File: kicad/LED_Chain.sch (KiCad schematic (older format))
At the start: 14 parts

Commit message: Schematic and initial layout
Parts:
- removed D? (x2): LED, symbol Device:LED
- added J1: Conn_01x07_Male, Pin_Headers:Pin_Header_Angled_1x07_Pitch2.54mm, symbol Connector:Conn_01x07_Male
- added J2: L1, Connect:Banana_Jack_1Pin, symbol Connector:Conn_01x01_Female
- added J3: L2, Connect:Banana_Jack_1Pin, symbol Connector:Conn_01x01_Female
- Q1, Q2, Q3, Q4: renamed from Q?; value Q_NMOS_GSD -> IRLML2502; footprint (none) -> TO_SOT_Packages_SMD:SOT-23
- R1, R2: renamed from R?; value R -> 10 kΩ; footprint (none) -> Resistors_SMD:R_0805
- R3, R4: renamed from R?; value R -> 27 Ω; footprint (none) -> Resistors_SMD:R_0805
- R5, R6: renamed from R?; value R -> 0 Ω; footprint (none) -> Resistors_SMD:R_0805
- U1: renamed from U?; value 4027 -> HCF4027B; footprint (none) -> SMD_Packages:SO-16-N
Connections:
- net labels added: CLK, GND, J, K, L1, L2, RESET, SET, Vdd
- wire segments 2 -> 45
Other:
- moved on the sheet: Q1, Q2, Q3, Q4, R1, R2, R3, R4, R5, R6, U1B, U1C

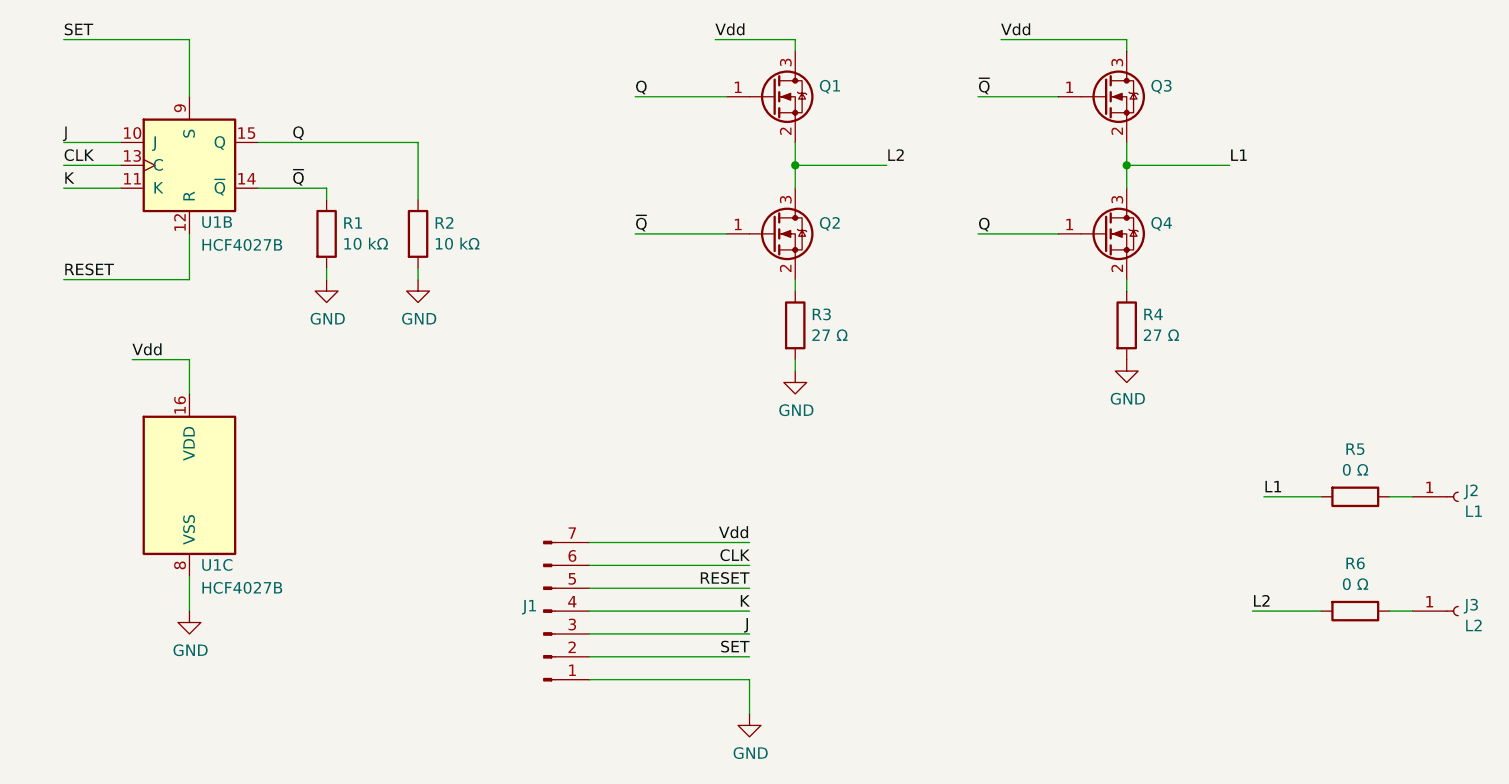
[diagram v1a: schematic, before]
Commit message: Added a buffer resitor to the gates
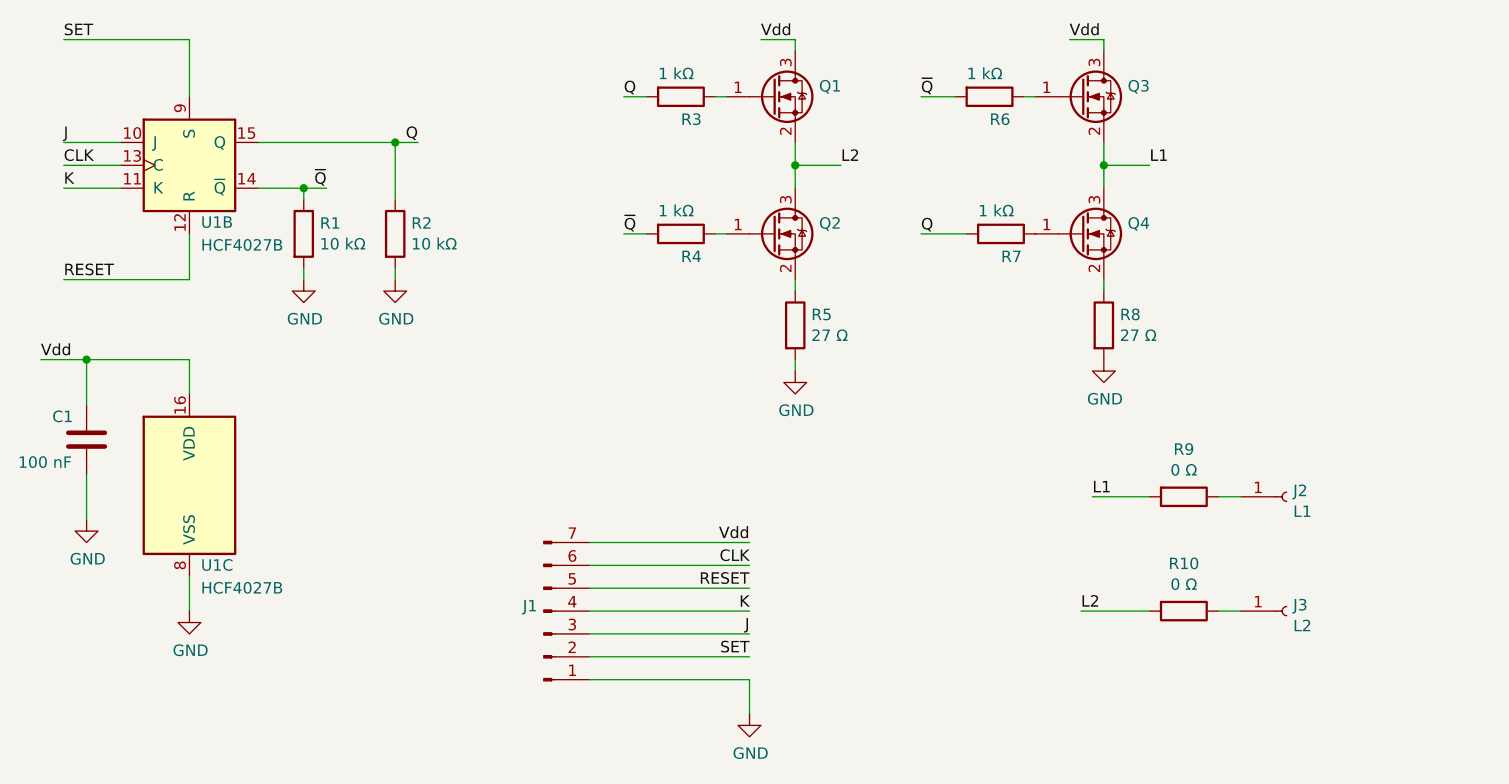
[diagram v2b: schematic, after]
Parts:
- added C1: 100 nF, Capacitors_SMD:C_0805, symbol Device:C
- added R3, R4, R6, R7: 1 kΩ, Resistors_SMD:R_0805, symbol Device:R
- renumbered R6 to R10, R3 to R5, R4 to R8, R5 to R9
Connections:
- net GND: now also C1.2
- net Q: now also R3.2, R7.2; no longer Q1.1 (G), Q4.1 (G)
- net Vdd: now also C1.1
- net ~Q: now also R4.2, R6.2; no longer Q2.1 (G), Q3.1 (G)
- new net: Q3.1 (G), R6.1
- new net: Q4.1 (G), R7.1
- new net: Q1.1 (G), R3.1
- new net: Q2.1 (G), R4.1
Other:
- moved on the sheet: J2, J3, Q3, Q4, R1, R10, R2, R8, R9

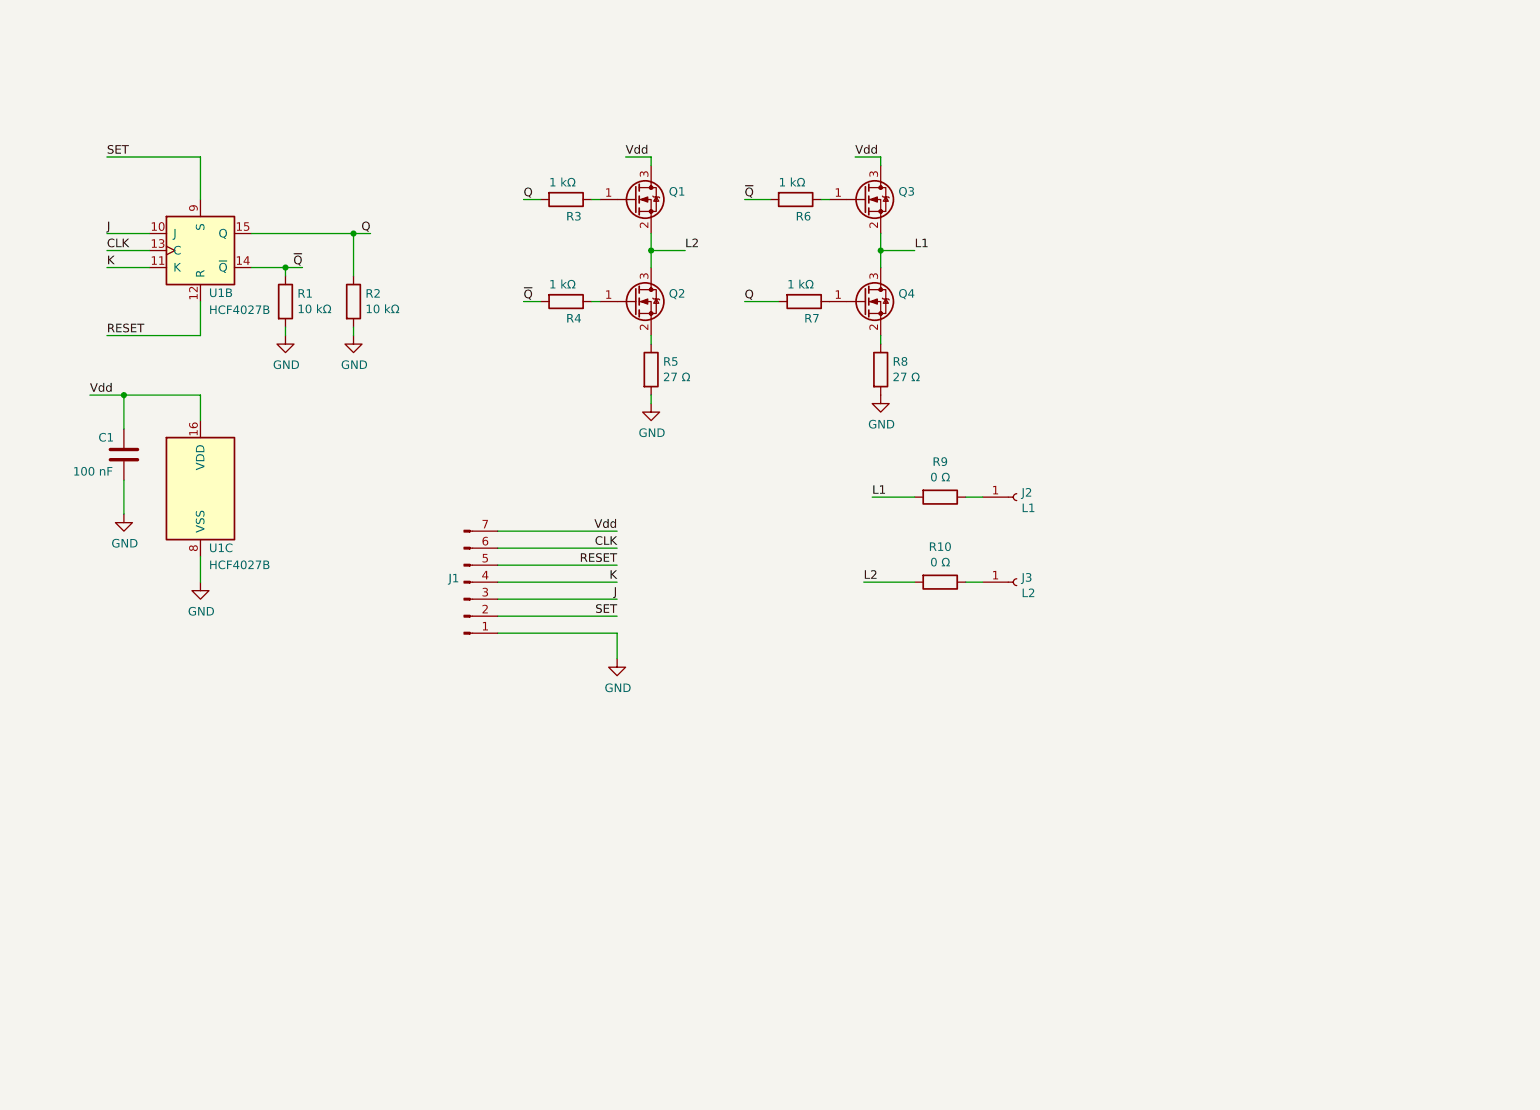
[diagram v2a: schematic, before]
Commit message: Updated the schematic and started a new layout for the final design
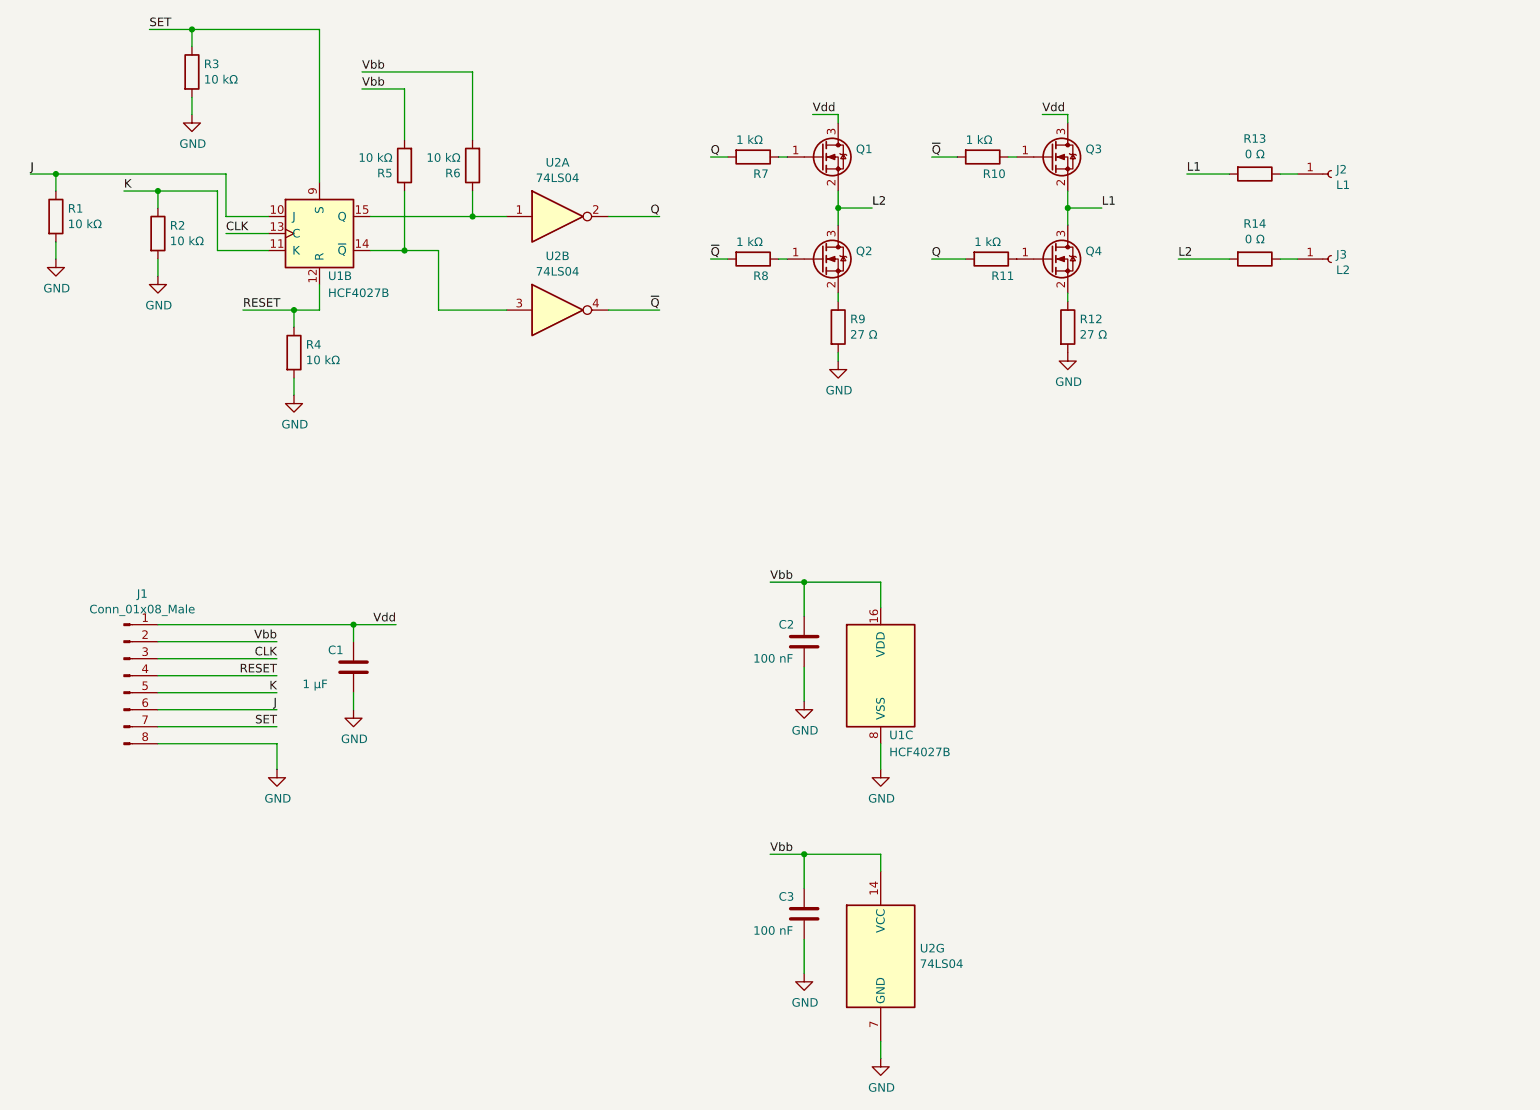
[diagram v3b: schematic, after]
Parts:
- removed J1: Conn_01x07_Male, Pin_Headers:Pin_Header_Angled_1x07_Pitch2.54mm, symbol Connector:Conn_01x07_Male
- added C1: 1 μF, Capacitors_SMD:C_0805, symbol Device:C
- added C3: 100 nF, Capacitors_SMD:C_0805, symbol Device:C
- added J1: Conn_01x08_Male, Pin_Headers:Pin_Header_Angled_1x08_Pitch2.54mm, symbol Connector:Conn_01x08_Male
- added R1, R2, R3, R4: 10 kΩ, Resistors_SMD:R_0805, symbol Device:R
- added U2: 74LS04, LED_Chain:SOIC-14, symbol 74xx:74LS04
- renumbered C1 to C2, R6 to R10, R7 to R11, R8 to R12, R9 to R13, R10 to R14, R2 to R5, R1 to R6, R3 to R7, R4 to R8, R5 to R9
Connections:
- net CLK: now also J1.3 (Pin_3)
- net GND: now also C1.2, C3.2, J1.8 (Pin_8), R1.2, R2.2, R3.2, R4.2, U2.7 (GND); no longer R5.2, R6.2
- net J: now also J1.6 (Pin_6), R1.1
- net K: now also J1.5 (Pin_5), R2.1
- net Q: now also U2.2; no longer R5.1, U1.15 (Q)
- net RESET: now also J1.4 (Pin_4), R4.1
- net SET: now also J1.7 (Pin_7), R3.1
- net Vdd: now also C1.1, J1.1 (Pin_1); no longer C2.1, U1.16 (VDD)
- net ~Q: now also U2.4; no longer R6.1, U1.14 (~Q)
- new net: R5.1, U1.14 (~Q), U2.3
- new net: R6.1, U1.15 (Q), U2.1
- new net Vbb: C2.1, C3.1, J1.2 (Pin_2), R5.2, R6.2, U1.16 (VDD), U2.14 (VCC)
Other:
- moved on the sheet: C2, J2, J3, Q1, Q2, Q3, Q4, R10, R11, R12, R13, R14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

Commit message: Another layout attempt - changes to pin layout for Neopixel interface
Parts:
- added J2: PWR, Pin_Headers:Pin_Header_Straight_1x02_Pitch2.54mm, symbol Connector:Conn_01x02_Male
- added J3: NeoPixel R1 A, Pin_Headers:Pin_Header_Straight_1x03_Pitch2.54mm, symbol Connector:Conn_01x03_Male
- added J4: NeoPixel R1 B, Pin_Headers:Pin_Header_Straight_1x04_Pitch2.54mm, symbol Connector:Conn_01x04_Male
- added J5: NeoPixel R1 C, Pin_Headers:Pin_Header_Straight_1x04_Pitch2.54mm, symbol Connector:Conn_01x04_Male
- added J6: NeoPixel R1 D, Pin_Headers:Pin_Header_Straight_1x02_Pitch2.54mm, symbol Connector:Conn_01x02_Male
- J1: value Conn_01x08_Male -> Interface
- renumbered J2 to J7, J3 to J8
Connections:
- net GND: now also J6.2 (Pin_2)
- net Vbb: now also J2.1 (Pin_1)
- net CLK renamed B0
- net B0: now also J5.4 (Pin_4)
- net J renamed A2
- net A2: now also J3.2 (Pin_2)
- net K renamed A3
- net A3: now also J3.1 (Pin_1)
- net RESET renamed A4
- net A4: now also J4.1 (Pin_1)
- net SET renamed A1
- net A1: now also J3.3 (Pin_3)
- net Vdd renamed 5V
- net 5V: now also J2.2 (Pin_2), J6.1 (Pin_1)
- new net A5: J4.2 (Pin_2)
- new net A6: J4.3 (Pin_3)
- new net A7: J4.4 (Pin_4)
- new net B1: J5.3 (Pin_3)
- new net B2: J5.2 (Pin_2)
- new net B3: J5.1 (Pin_1)
- no-connect marks 0 -> 6
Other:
- note added: "Interface to the NeoPixel R 2L_1"
- note added: "Jumper for common Vbb and Vdd"
- moved on the sheet: C1, C2, C3, U1C, U2G

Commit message: Completed the layout
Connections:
- net B0: now also J5.1 (Pin_1); no longer J5.4 (Pin_4)
- net B1: now also J5.2 (Pin_2); no longer J5.3 (Pin_3)
- net B2: now also J5.3 (Pin_3); no longer J5.2 (Pin_2)
- net B3: now also J5.4 (Pin_4); no longer J5.1 (Pin_1)
- net Q: now also U2.12; no longer U2.2
- net ~Q: now also U2.10; no longer U2.4
- net at R5.1, U1.14 (~Q): now also U2.11; no longer U2.3
- net at R6.1, U1.15 (Q): now also U2.13; no longer U2.1
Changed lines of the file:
@@
 $Comp
 L 74xx:74LS04 U2
-U 1 1 5FA1C3A1
+U 6 1 5FA1C3A1
 P 3800 2050
 F 0 "U2" H 3800 2367 50  0000 C CNN
@@
 F 2 "LED_Chain:SOIC-14" H 3800 2050 50  0001 C CNN
 F 3 "http://www.ti.com/lit/gpn/sn74LS04" H 3800 2050 50  0001 C CNN
-	1    3800 2050
+	6    3800 2050
 	1    0    0    -1
 $EndComp
 $Comp
 L 74xx:74LS04 U2
-U 2 1 5FA1F249
+U 5 1 5FA1F249
 P 3800 2600
 F 0 "U2" H 3800 2917 50  0000 C CNN
@@
 F 2 "LED_Chain:SOIC-14" H 3800 2600 50  0001 C CNN
 F 3 "http://www.ti.com/lit/gpn/sn74LS04" H 3800 2600 50  0001 C CNN
-	2    3800 2600
+	5    3800 2600
 	1    0    0    -1
 $EndComp
@@
 Connection ~ 850  1800
 Wire Wire Line
-	850  1800 700  1800
-Text Label 700  1800 0    50   ~ 0
+	850  1800 600  1800
+Text Label 600  1800 0    50   ~ 0
 FF_J
 Wire Wire Line
@@
 Text Label 7350 4850 0    50   ~ 0
 A7
+Text Label 7350 5250 0    50   ~ 0
+B3
+Text Label 7350 5150 0    50   ~ 0
+B2
+Text Label 7350 5050 0    50   ~ 0
+B1
 Text Label 7350 4950 0    50   ~ 0
-B3
-Text Label 7350 5050 0    50   ~ 0
-B2
-Text Label 7350 5150 0    50   ~ 0
-B1
-Text Label 7350 5250 0    50   ~ 0
 B0
 Text Label 7350 4250 0    50   ~ 0
@@
 Text Label 7350 5350 0    50   ~ 0
 5V
-Text Label 7350 5450 0    50   ~ 0
+Text Label 6850 5450 0    50   ~ 0
 GND
 $Comp
@@
 Wire Wire Line
 	7550 5150 6850 5150
-Text Label 6850 5250 0    50   ~ 0
+Text Label 6850 4950 0    50   ~ 0
 CLK
 Text Label 6850 4350 0    50   ~ 0
@@
 NoConn ~ 6850 4750
 NoConn ~ 6850 4850
-NoConn ~ 6850 4950
+NoConn ~ 6850 5250
 NoConn ~ 6850 5050
 NoConn ~ 6850 5150

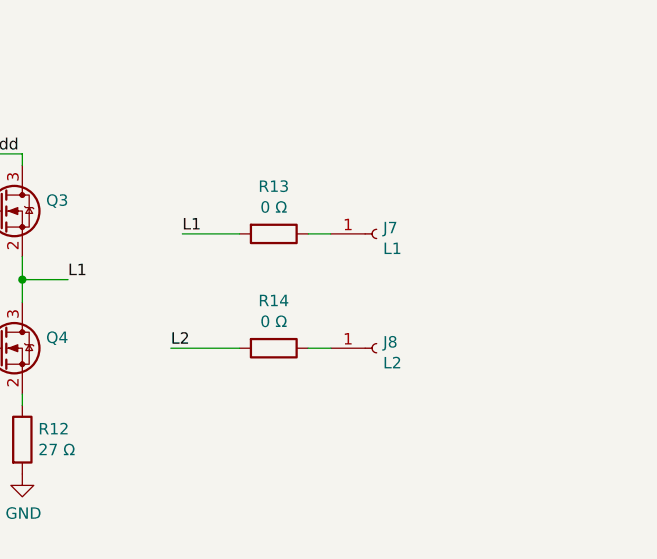
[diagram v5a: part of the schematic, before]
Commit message: Completed layout and sent to OSH Park
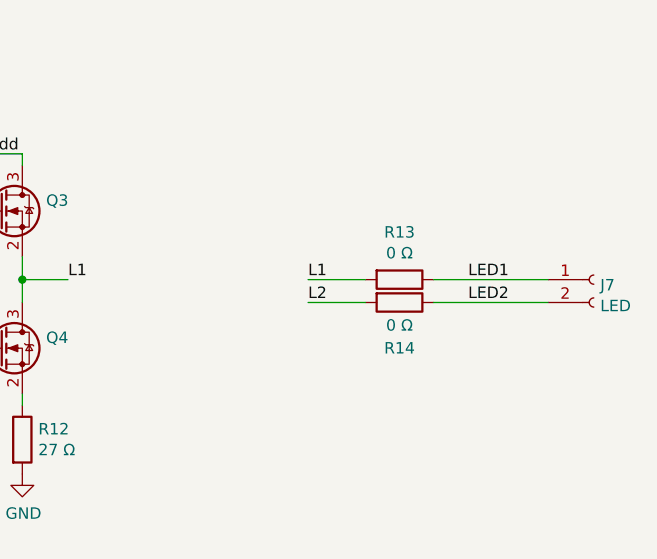
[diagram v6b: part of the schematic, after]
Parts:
- removed J7: L1, Connect:Banana_Jack_1Pin, symbol Connector:Conn_01x01_Female
- removed J8: L2, Connect:Banana_Jack_1Pin, symbol Connector:Conn_01x01_Female
- added J7: LED, LED_Chain:TerminalBlock_bornier-2_P5.08mm, symbol Connector:Conn_01x02_Female
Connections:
- net LED1: now reaches R13.1
- net LED1: now also J7.1 (Pin_1)
- net LED2: now reaches R14.1
- net LED2: now also J7.2 (Pin_2)
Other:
- moved on the sheet: R13, R14
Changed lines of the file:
@@
 L Device:R R13
 U 1 1 5F916E87
-P 7900 1800
-F 0 "R13" V 7693 1800 50  0000 C CNN
-F 1 "0 Ω" V 7784 1800 50  0000 C CNN
-F 2 "Resistors_SMD:R_0805" V 7830 1800 50  0001 C CNN
-F 3 "~" H 7900 1800 50  0001 C CNN
-	1    7900 1800
+P 8450 2000
+F 0 "R13" V 8243 2000 50  0000 C CNN
+F 1 "0 Ω" V 8334 2000 50  0000 C CNN
+F 2 "Resistors_SMD:R_0805" V 8380 2000 50  0001 C CNN
+F 3 "~" H 8450 2000 50  0001 C CNN
+	1    8450 2000
 	0    1    1    0
 $EndComp
@@
 L Device:R R14
 U 1 1 5F917A36
-P 7900 2300
-F 0 "R14" V 7693 2300 50  0000 C CNN
-F 1 "0 Ω" V 7784 2300 50  0000 C CNN
-F 2 "Resistors_SMD:R_0805" V 7830 2300 50  0001 C CNN
-F 3 "~" H 7900 2300 50  0001 C CNN
-	1    7900 2300
+P 8450 2100
+F 0 "R14" V 8650 2100 50  0000 C CNN
+F 1 "0 Ω" V 8550 2100 50  0000 C CNN
+F 2 "Resistors_SMD:R_0805" V 8380 2100 50  0001 C CNN
+F 3 "~" H 8450 2100 50  0001 C CNN
+	1    8450 2100
 	0    1    1    0
 $EndComp
@@
 	5450 2000 5450 2100
 Wire Wire Line
-	7750 2300 7450 2300
-Wire Wire Line
-	7750 1800 7500 1800
-Text Label 7500 1800 0    50   ~ 0
+	8300 2100 8050 2100
+Wire Wire Line
+	8300 2000 8050 2000
+Text Label 8050 2000 0    50   ~ 0
 L1
-Text Label 7450 2300 0    50   ~ 0
+Text Label 8050 2100 0    50   ~ 0
 L2
 Text Label 7000 2000 0    50   ~ 0
@@
 Vdd
 Wire Wire Line
-	8050 1800 8150 1800
-Wire Wire Line
-	8050 2300 8150 2300
-$Comp
-L Connector:Conn_01x01_Female J7
-U 1 1 5F981829
-P 8350 1800
-F 0 "J7" H 8378 1826 50  0000 L CNN
-F 1 "L1" H 8378 1735 50  0000 L CNN
-F 2 "Connect:Banana_Jack_1Pin" H 8350 1800 50  0001 C CNN
-F 3 "~" H 8350 1800 50  0001 C CNN
-	1    8350 1800
-	1    0    0    -1
-$EndComp
-$Comp
-L Connector:Conn_01x01_Female J8
-U 1 1 5F981CC7
-P 8350 2300
-F 0 "J8" H 8378 2326 50  0000 L CNN
-F 1 "L2" H 8378 2235 50  0000 L CNN
-F 2 "Connect:Banana_Jack_1Pin" H 8350 2300 50  0001 C CNN
-F 3 "~" H 8350 2300 50  0001 C CNN
-	1    8350 2300
-	1    0    0    -1
-$EndComp
+	8600 2000 9100 2000
+Wire Wire Line
+	8600 2100 9100 2100
 Wire Wire Line
 	1700 5150 1700 5300
@@
 Wire Wire Line
 	1450 4550 2350 4550
+$Comp
+L Connector:Conn_01x02_Female J7
+U 1 1 5FAA49F0
+P 9300 2000
+F 0 "J7" H 9328 1976 50  0000 L CNN
+F 1 "LED" H 9328 1885 50  0000 L CNN
+F 2 "LED_Chain:TerminalBlock_bornier-2_P5.08mm" H 9300 2000 50  0001 C CNN
+F 3 "~" H 9300 2000 50  0001 C CNN
+	1    9300 2000
+	1    0    0    -1
+$EndComp
+Text Label 8750 2000 0    50   ~ 0
+LED1
+Text Label 8750 2100 0    50   ~ 0
+LED2
 $EndSCHEMATC
